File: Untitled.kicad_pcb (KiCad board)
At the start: 2 copper layers, 37.5 x 34.5 mm, 5 parts, among them SW1 SW_Push

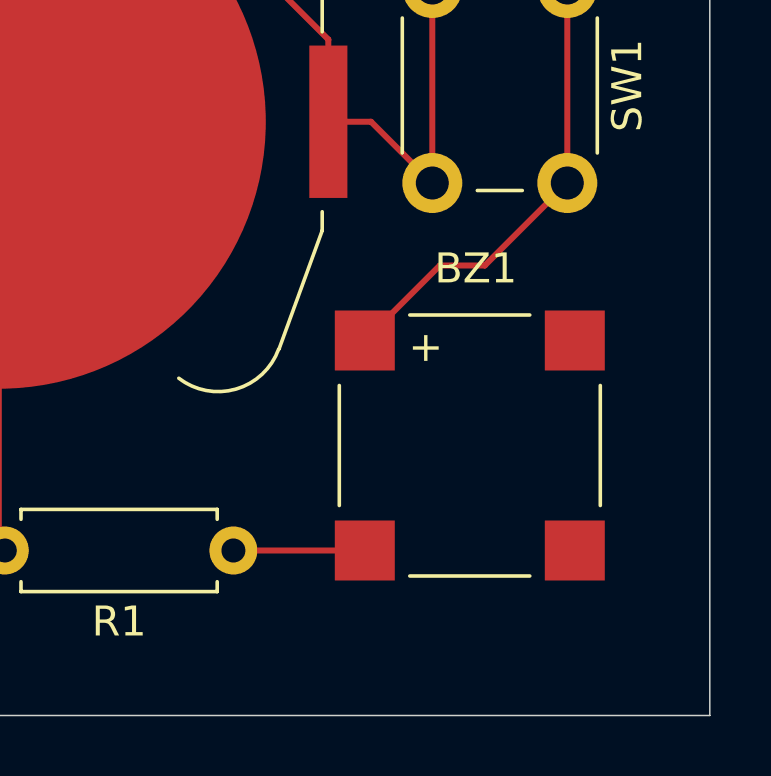
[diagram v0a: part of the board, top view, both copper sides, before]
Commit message: Added logo to schematic
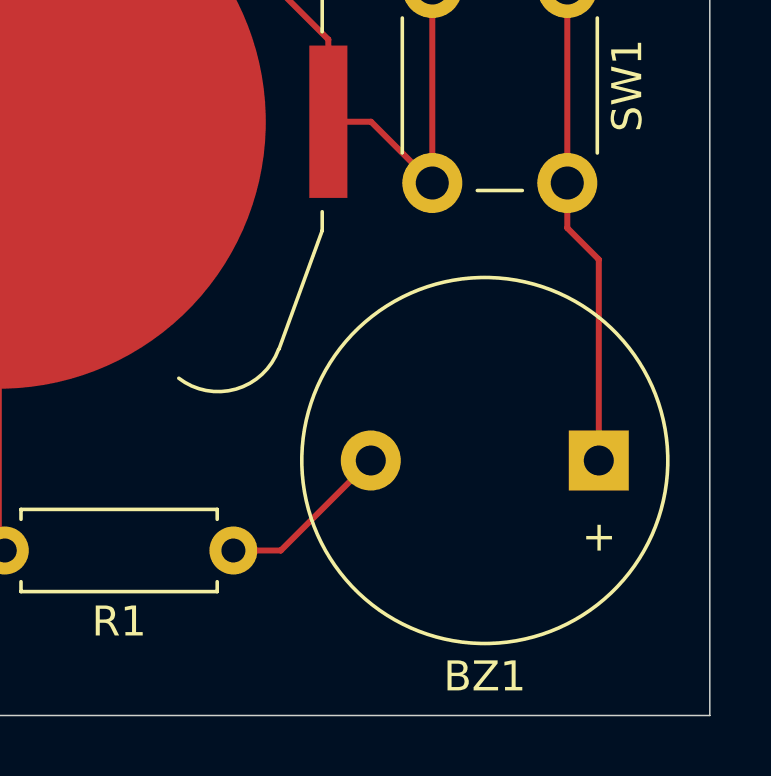
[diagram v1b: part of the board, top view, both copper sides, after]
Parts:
- BZ1: footprint Buzzer_Beeper:PUIAudio_SMT_0825_S_4_R -> Buzzer_Beeper:Buzzer_12x9.5RM7.6
- moved BZ1 4.33 mm to (164.3, 108.0), turned to 180 degrees
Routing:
- net Net-(BZ1--): track 4.38 -> 5.82 mm
- net Net-(BZ1-+): track 15.4 -> 16.2 mm
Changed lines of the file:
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@@
 		)
 	)
-	(footprint "Buzzer_Beeper:PUIAudio_SMT_0825_S_4_R"
-		(layer "F.Cu")
-		(at 160 107.5)
-		(descr "SMD 8540, http://www.puiaudio.com/product-detail.aspx?partnumber=SMT-0825-S-4-R")
-		(tags "SMD 8540")
+	(footprint "Buzzer_Beeper:Buzzer_12x9.5RM7.6"
+		(layer "F.Cu")
+		(at 164.3 108 180)
+		(descr "Generic Buzzer, D12mm height 9.5mm with RM7.6mm")
+		(tags "buzzer")
 		(property "Reference" "BZ1"
-			(at 0.2 -5.9 0)
+			(at 3.8 -7.2 0)
 			(layer "F.SilkS")
 			(effects
@@
 		)
 		(property "Value" "Buzzer"
-			(at 0.1 6 0)
+			(at 3.8 7.4 0)
 			(layer "F.Fab")
 			(effects
@@
 		)
 		(property "Datasheet" ""
-			(at 0 0 0)
+			(at 0 0 180)
 			(unlocked yes)
 			(layer "F.Fab")
@@
 		)
 		(property "Description" "Buzzer, polarized"
-			(at 0 0 0)
+			(at 0 0 180)
 			(unlocked yes)
 			(layer "F.Fab")
@@
 		(sheetname "/")
 		(sheetfile "Untitled.kicad_sch")
-		(attr smd)
-		(fp_line
-			(start -4.35 -2)
-			(end -4.35 2)
+		(attr through_hole)
+		(fp_circle
+			(center 3.8 0)
+			(end 9.9 0)
 			(stroke
 				(width 0.12)
 				(type solid)
 			)
+			(fill no)
 			(layer "F.SilkS")
 		)
-		(fp_line
-			(start -2 4.35)
-			(end 2 4.35)
-			(stroke
-				(width 0.12)
-				(type solid)
-			)
+		(fp_circle
+			(center 3.8 0)
+			(end 10.05 0)
+			(stroke
+				(width 0.05)
+				(type solid)
+			)
+			(fill no)
+			(layer "F.CrtYd")
+		)
+		(fp_circle
+			(center 3.8 0)
+			(end 9.8 0)
+			(stroke
+				(width 0.1)
+				(type solid)
+			)
+			(fill no)
+			(layer "F.Fab")
+		)
+		(fp_circle
+			(center 3.8 0)
+			(end 4.8 0)
+			(stroke
+				(width 0.1)
+				(type solid)
+			)
+			(fill no)
+			(layer "F.Fab")
+		)
+		(fp_text user "+"
+			(at -0.01 -2.54 0)
 			(layer "F.SilkS")
-		)
-		(fp_line
-			(start 2 -4.35)
-			(end -2 -4.35)
-			(stroke
-				(width 0.12)
-				(type solid)
-			)
-			(layer "F.SilkS")
-		)
-		(fp_line
-			(start 4.35 2)
-			(end 4.35 -2)
-			(stroke
-				(width 0.12)
-				(type solid)
-			)
-			(layer "F.SilkS")
-		)
-		(fp_line
-			(start -4.75 -4.75)
-			(end 4.75 -4.75)
-			(stroke
-				(width 0.05)
-				(type solid)
-			)
-			(layer "F.CrtYd")
-		)
-		(fp_line
-			(start -4.75 4.75)
-			(end -4.75 -4.75)
-			(stroke
-				(width 0.05)
-				(type solid)
-			)
-			(layer "F.CrtYd")
-		)
-		(fp_line
-			(start 4.75 -4.75)
-			(end 4.75 4.75)
-			(stroke
-				(width 0.05)
-				(type solid)
-			)
-			(layer "F.CrtYd")
-		)
-		(fp_line
-			(start 4.75 4.75)
-			(end -4.75 4.75)
-			(stroke
-				(width 0.05)
-				(type solid)
-			)
-			(layer "F.CrtYd")
-		)
-		(fp_line
-			(start -4.25 -2.75)
-			(end -2.75 -4.25)
-			(stroke
-				(width 0.1)
-				(type solid)
-			)
-			(layer "F.Fab")
-		)
-		(fp_line
-			(start -4.25 2.75)
-			(end -4.25 -2.75)
-			(stroke
-				(width 0.1)
-				(type solid)
-			)
-			(layer "F.Fab")
-		)
-		(fp_line
-			(start -2.75 -4.25)
-			(end 2.75 -4.25)
-			(stroke
-				(width 0.1)
-				(type solid)
-			)
-			(layer "F.Fab")
-		)
-		(fp_line
-			(start -2.75 4.25)
-			(end -4.25 2.75)
-			(stroke
-				(width 0.1)
-				(type solid)
-			)
-			(layer "F.Fab")
-		)
-		(fp_line
-			(start 2.75 -4.25)
-			(end 4.25 -2.75)
-			(stroke
-				(width 0.1)
-				(type solid)
-			)
-			(layer "F.Fab")
-		)
-		(fp_line
-			(start 2.75 4.25)
-			(end -2.75 4.25)
-			(stroke
-				(width 0.1)
-				(type solid)
-			)
-			(layer "F.Fab")
-		)
-		(fp_line
-			(start 4.25 -2.75)
-			(end 4.25 2.75)
-			(stroke
-				(width 0.1)
-				(type solid)
-			)
-			(layer "F.Fab")
-		)
-		(fp_line
-			(start 4.25 2.75)
-			(end 2.75 4.25)
-			(stroke
-				(width 0.1)
-				(type solid)
-			)
-			(layer "F.Fab")
+			(effects
+				(font
+					(size 1 1)
+					(thickness 0.15)
+				)
+			)
+		)
+		(fp_text user "${REFERENCE}"
+			(at 3.8 -4 0)
+			(layer "F.Fab")
+			(effects
+				(font
+					(size 1 1)
+					(thickness 0.15)
+				)
+			)
 		)
 		(fp_text user "+"
-			(at -1.5 -3.25 270)
-			(layer "F.SilkS")
+			(at -0.01 -2.54 0)
+			(layer "F.Fab")
 			(effects
 				(font
@@
 			)
 		)
-		(fp_text user "${REFERENCE}"
-			(at 0.1 0.1 0)
-			(layer "F.Fab")
-			(effects
-				(font
-					(size 1 1)
-					(thickness 0.15)
-				)
-			)
-		)
-		(fp_text user "+"
-			(at -2.75 -2.75 270)
-			(layer "F.Fab")
-			(effects
-				(font
-					(size 1 1)
-					(thickness 0.15)
-				)
-			)
-		)
-		(pad "1" smd rect
-			(at -3.5 -3.5 270)
+		(pad "1" thru_hole rect
+			(at 0 0 180)
 			(size 2 2)
-			(layers "F.Cu" "F.Mask" "F.Paste")
+			(drill 1)
+			(layers "*.Cu" "*.Mask")
+			(remove_unused_layers no)
 			(net 3 "Net-(BZ1-+)")
 			(pinfunction "+")
 			(pintype "passive")
 		)
-		(pad "2" smd rect
-			(at -3.5 3.5 270)
+		(pad "2" thru_hole circle
+			(at 7.6 0 180)
 			(size 2 2)
-			(layers "F.Cu" "F.Mask" "F.Paste")
+			(drill 1)
+			(layers "*.Cu" "*.Mask")
+			(remove_unused_layers no)
 			(net 4 "Net-(BZ1--)")
 			(pinfunction "-")
 			(pintype "passive")
 		)
-		(pad "3" smd rect
-			(at 3.5 3.5 270)
-			(size 2 2)
-			(layers "F.Cu" "F.Mask" "F.Paste")
-		)
-		(pad "4" smd rect
-			(at 3.5 -3.5 270)
-			(size 2 2)
-			(layers "F.Cu" "F.Mask" "F.Paste")
-		)
 		(embedded_fonts no)
-		(model "${KICAD9_3DMODEL_DIR}/Buzzer_Beeper.3dshapes/PUIAudio_SMT_0825_S_4_R.wrl"
+		(model "${KICAD9_3DMODEL_DIR}/Buzzer_Beeper.3dshapes/Buzzer_12x9.5RM7.6.wrl"
 			(offset
 				(xyz 0 0 0)
@@
 	)
 	(segment
-		(start 159 101.5)
-		(end 156.5 104)
+		(start 164.3 101.3)
+		(end 164.3 108)
 		(width 0.2)
 		(layer "F.Cu")
@@
 	)
 	(segment
+		(start 163.25 100.25)
+		(end 164.3 101.3)
+		(width 0.2)
+		(layer "F.Cu")
+		(net 3)
+	)
+	(segment
 		(start 163.25 98.75)
-		(end 160.5 101.5)
+		(end 163.25 100.25)
 		(width 0.2)
 		(layer "F.Cu")
@@
 	)
 	(segment
-		(start 160.5 101.5)
-		(end 159 101.5)
-		(width 0.2)
-		(layer "F.Cu")
-		(net 3)
-	)
-	(segment
 		(start 152.12 111)
-		(end 156.5 111)
-		(width 0.2)
-		(layer "F.Cu")
+		(end 153.7 111)
+		(width 0.2)
+		(layer "F.Cu")
+		(net 4)
+	)
+	(segment
+		(start 153.7 111)
+		(end 156.7 108)
+		(width 0.2)
+		(layer "F.Cu")

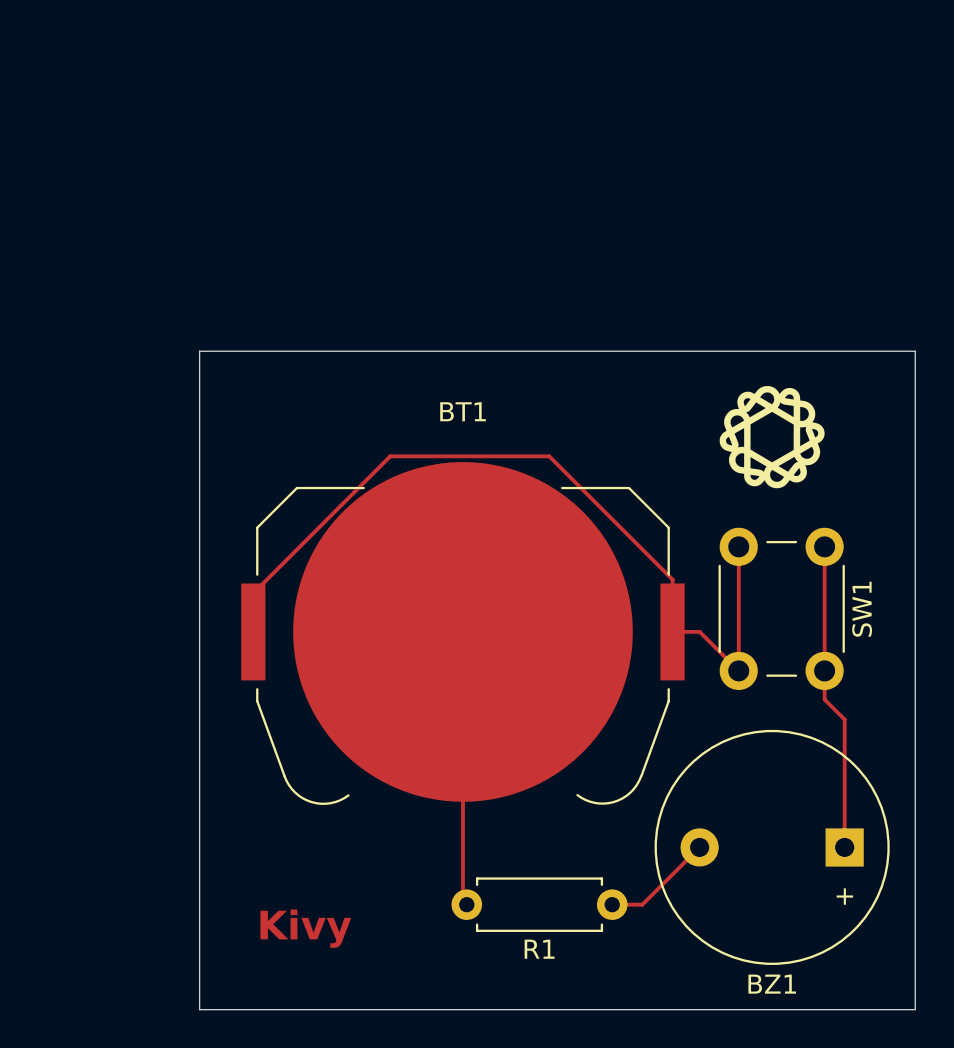
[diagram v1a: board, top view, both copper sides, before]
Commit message: Added LEDs
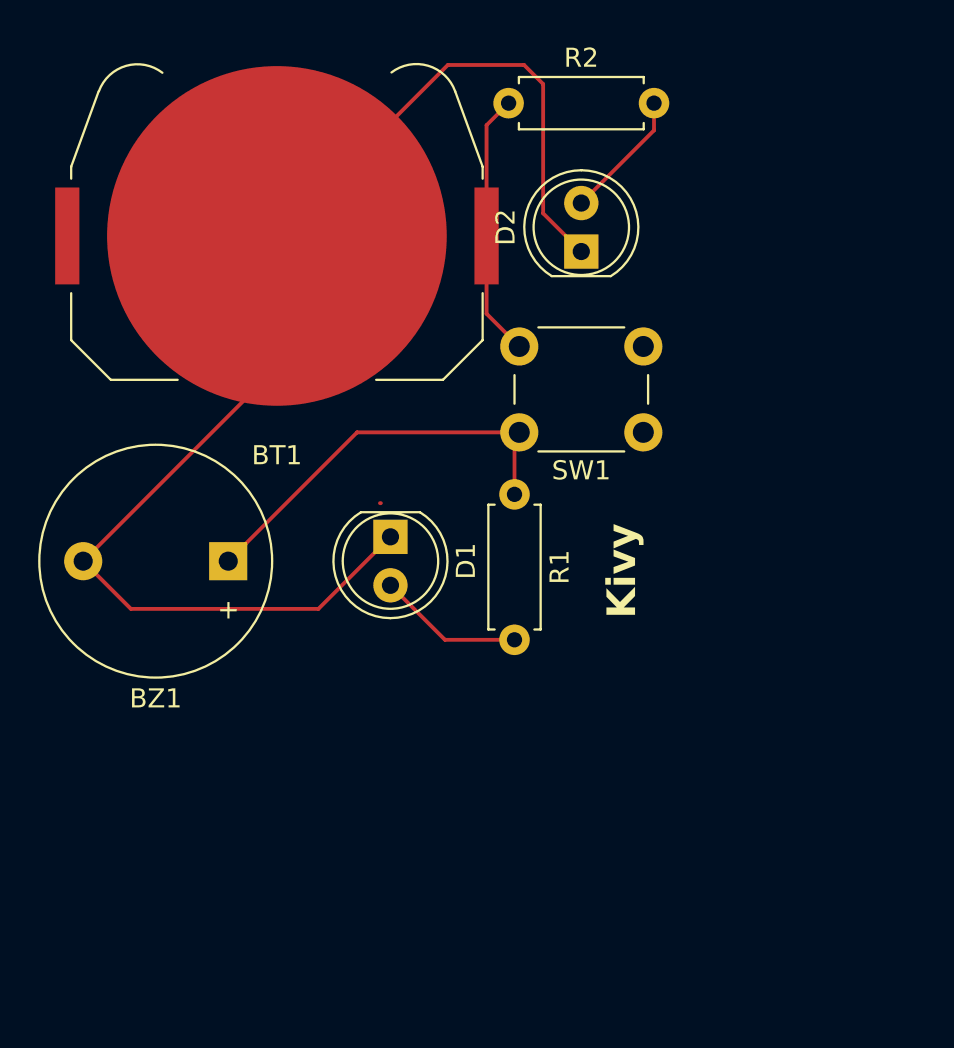
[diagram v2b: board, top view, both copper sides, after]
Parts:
- added D1: LED, LED_THT:LED_D5.0mm, F.Cu at (140.5, 91.7)
- added D2: LED, LED_THT:LED_D5.0mm, F.Cu at (150.5, 76.8)
- added R2: R, Resistor_THT:R_Axial_DIN0207_L6.3mm_D2.5mm_P7.62mm_Horizontal, F.Cu at (146.7, 69.0)
- G***: moved to B.Cu
- moved BZ1 35.6 mm to (132.0, 93.0)
- moved G*** 27.7 mm to (134.5, 77.0), turned to 180 degrees
- moved BT1 22.9 mm to (134.6, 76.0), turned to 180 degrees
- moved R1 22.1 mm to (147.0, 89.5), turned to -90 degrees
- moved SW1 11.2 mm to (153.8, 86.2), turned to 180 degrees
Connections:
- BZ1 pad 2: Net-(BZ1--) -> Net-(BT1--)
- R1 pad 1: Net-(BZ1--) -> Net-(BZ1-+)
- R1 pad 2: Net-(BT1--) -> Net-(D1-A)
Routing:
- net Net-(BT1--): track 14.4 -> 76.1 mm
- net Net-(BT1-+): track 43.2 -> 13.9 mm
- net Net-(D1-A): track 0.00 -> 7.68 mm
- net Net-(D2-A): track 0.00 -> 6.81 mm
- net Net-(BZ1--): track 5.82 -> 0.00 mm
- net Net-(BZ1-+): track 16.2 -> 21.4 mm
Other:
- board outline removed
